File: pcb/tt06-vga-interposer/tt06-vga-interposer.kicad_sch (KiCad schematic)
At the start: 71 parts, among them CON1 Bottom pins, CON2 Bottom pins, CON3 Top socket, CON4 Top socket, J1 Conn_02x09_Odd_Even, J2 DE15_Receptacle_HighDensity_M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, J3 Conn_01x04_Pin, J4 Conn_01x04_Pin, U1 OPA3355EA, U2 SN74ALVC245DWR

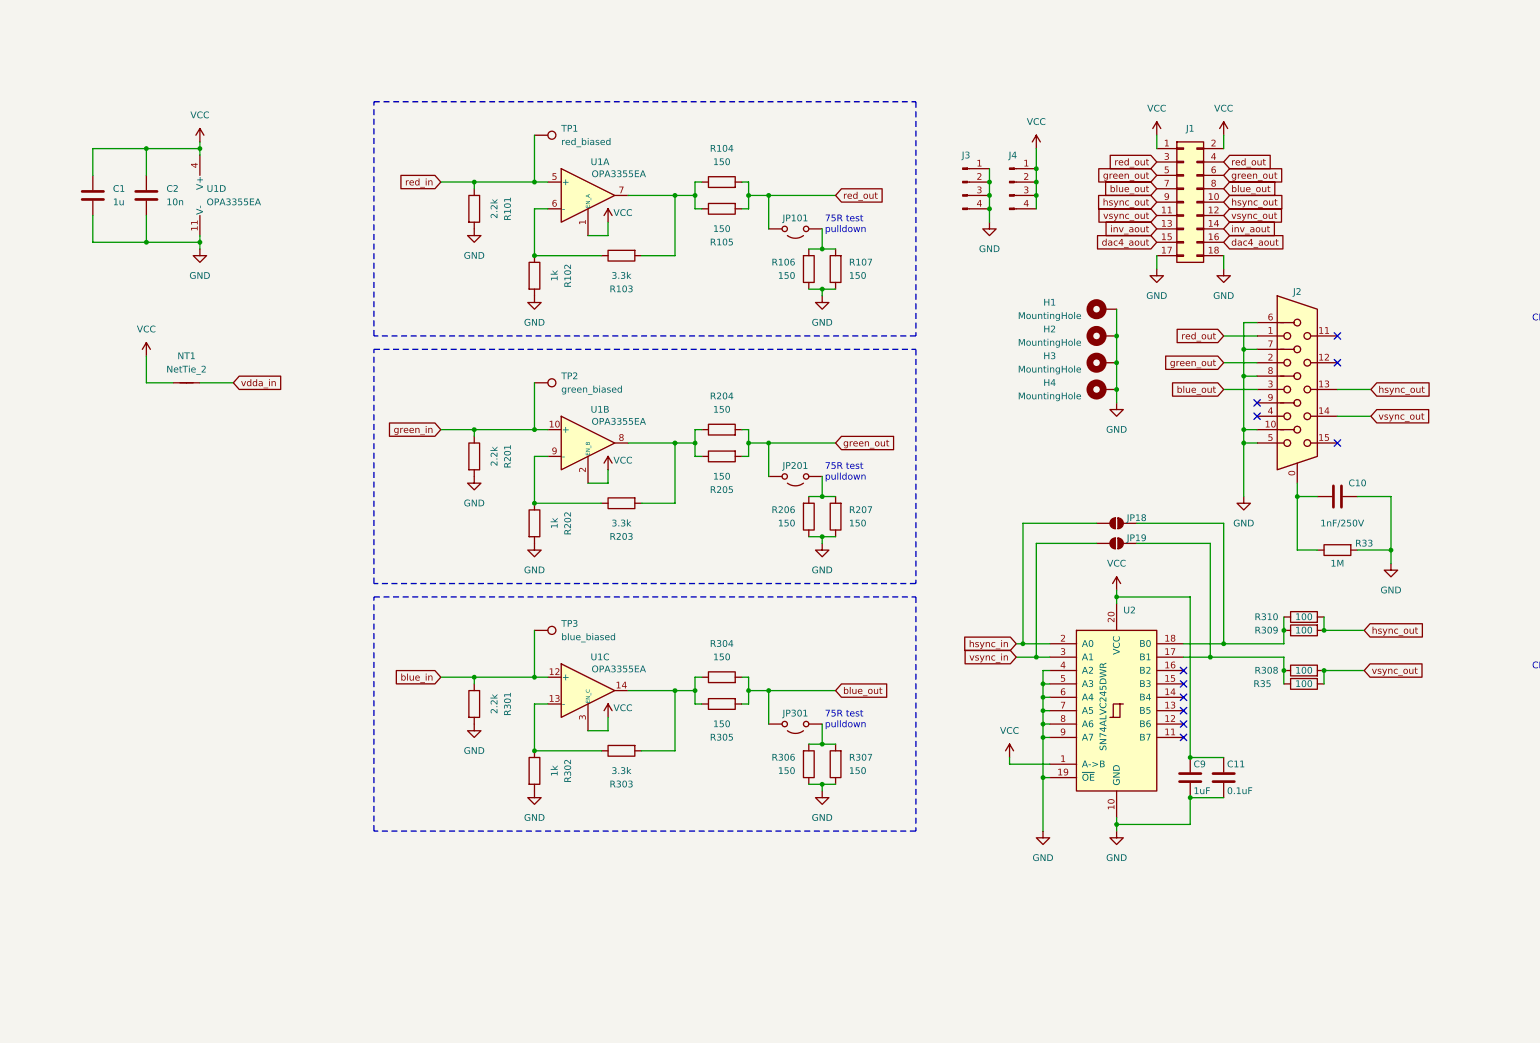
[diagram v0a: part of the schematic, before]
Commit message: Partial layout of interposer PCB
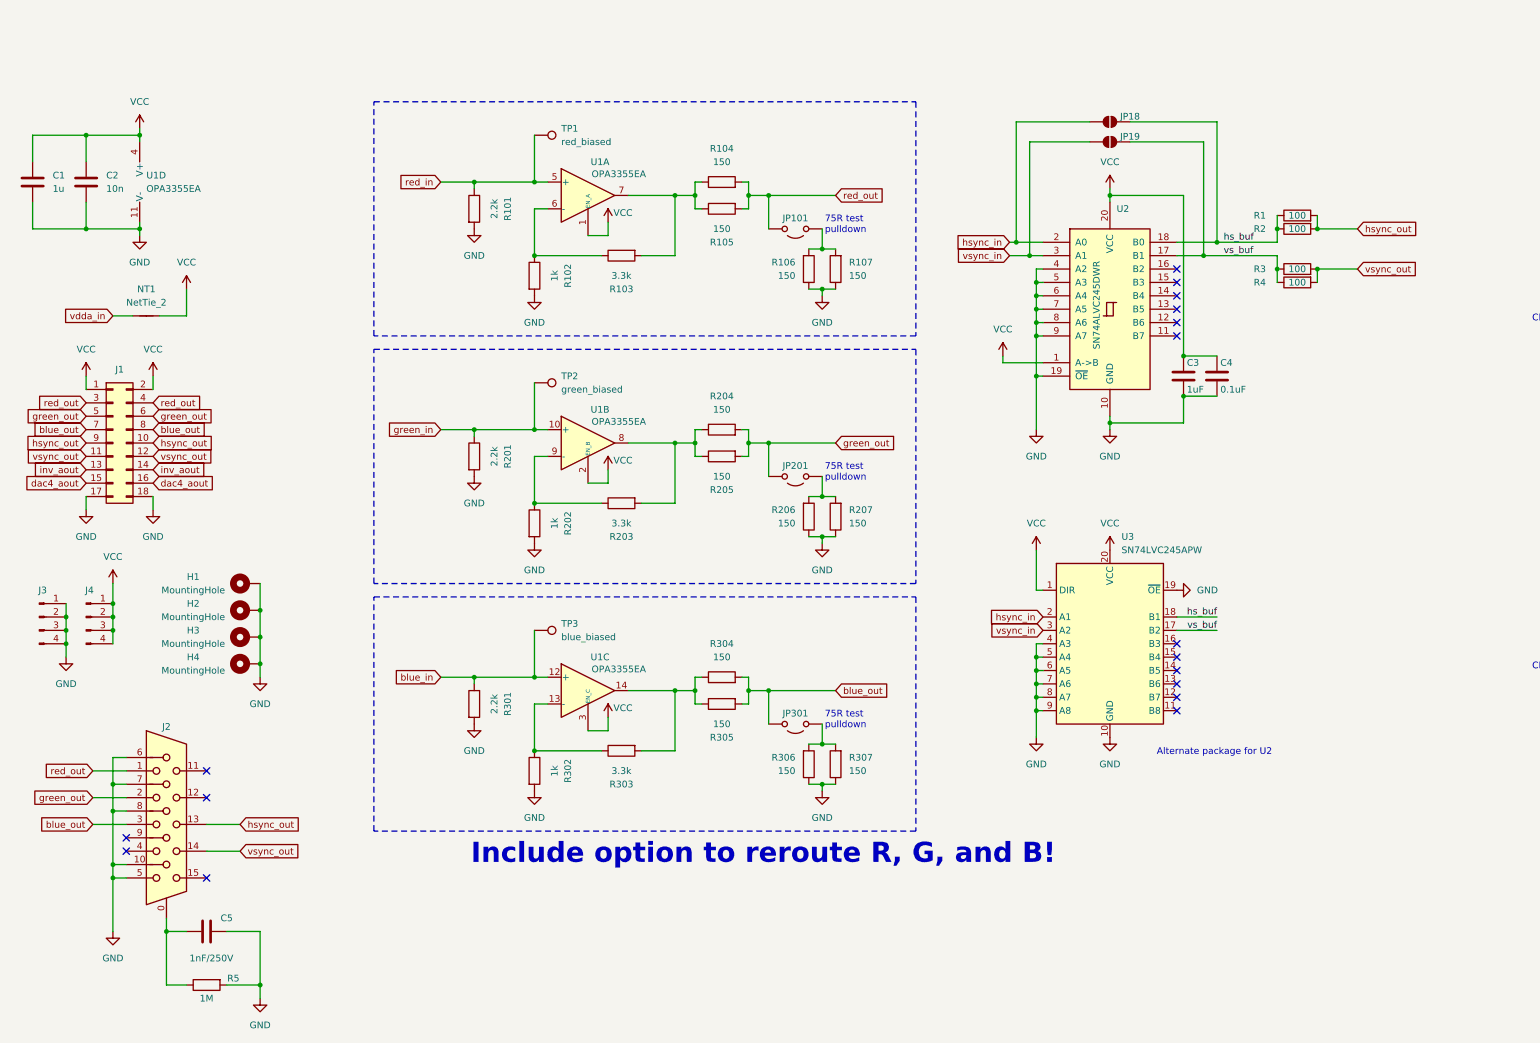
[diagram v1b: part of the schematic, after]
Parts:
- added U3: SN74LVC245APW, Anton Kicad Footprints Lib:TSSOP-20_4.4x6.5mm_P0.65mm_HandSolder, symbol Logic_LevelTranslator:SN74LVC245APW
- J1: footprint (none) -> Connector_PinHeader_2.54mm:PinHeader_2x09_P2.54mm_Horizontal
- renumbered C9 to C3, C11 to C4, C10 to C5, R310 to R1, R309 to R2, R308 to R3, R35 to R4, R33 to R5
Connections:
- net GND: now also U3.10 (GND), U3.19 (~{OE}), U3.4 (A3), U3.5 (A4), U3.6 (A5), U3.7 (A6), U3.8 (A7), U3.9 (A8)
- net VCC: now also U3.1 (DIR), U3.20 (VCC)
- net hsync_in: now also U3.2 (A1)
- net vsync_in: now also U3.3 (A2)
- net vs_buf: now reaches JP19.2 (B), R3.1, R4.1, U2.17 (B1)
- net vs_buf: now also U3.17 (B2)
- net hs_buf: now reaches JP18.2 (B), R1.1, R2.1, U2.18 (B0)
- net hs_buf: now also U3.18 (B1)
- no-connect marks 11 -> 17
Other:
- note added: "Alternate package for U2"
- note added: "Include option to reroute R, G, and B!"
- moved on the sheet: C1, C2, C3, C4, C5, H1, H2, H3, H4, J1, J2, J3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

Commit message: Nearly finished 1st draft of interposer PCB
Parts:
- removed JP13, JP14: SolderJumper_2_Open, Anton Kicad Footprints Lib:SolderJumper-2_tiny_nomask, symbol Jumper:SolderJumper_2_Open
- removed U2: SN74ALVC245DWR, Package_SO:SOIC-20W_7.5x12.8mm_P1.27mm, symbol Anton Kicad Symbols Lib:SN74ALVC245DWR
- added J5: Conn_02x07_Odd_Even, Connector_PinHeader_2.54mm:PinHeader_2x07_P2.54mm_Horizontal, symbol Connector_Generic:Conn_02x07_Odd_Even
- added JP16: SolderJumper_2_Open, Anton Kicad Footprints Lib:SolderJumper-2_tiny_nomask, symbol Jumper:SolderJumper_2_Open
- added NT2, NT3: NetTie_2, NetTie:NetTie-2_SMD_Pad0.5mm, symbol Device:NetTie_2
- JP101, JP201, JP301, R106, R107, R206, R207, R306, R307, TP1, TP2, TP3: now not fitted
- renumbered JP16 to JP13, JP17 to JP14, JP18 to JP17, JP19 to JP18, U3 to U2
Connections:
- net GND: now also J1.1 (Pin_1), J1.2 (Pin_2); no longer J1.17 (Pin_17), J1.18 (Pin_18)
- net VCC: now also J1.17 (Pin_17), J1.18 (Pin_18); no longer J1.1 (Pin_1), J1.2 (Pin_2)
- net blue_in: now also J5.11 (Pin_11); no longer JP15.2 (B)
- net blue_out: now also J1.11 (Pin_11), J1.12 (Pin_12); no longer J1.7 (Pin_7), J1.8 (Pin_8)
- net chip_an0: now also J5.12 (Pin_12), J5.4 (Pin_4), J5.8 (Pin_8)
- net chip_an4: now also J5.13 (Pin_13), J5.5 (Pin_5); no longer JP15.1 (A)
- net chip_an5: now also J5.1 (Pin_1), J5.9 (Pin_9)
- net dac4_aout: now also J1.5 (Pin_5), J1.6 (Pin_6); no longer J1.15 (Pin_15), J1.16 (Pin_16)
- net green_in: now also J5.7 (Pin_7)
- net green_out: now also J1.13 (Pin_13), J1.14 (Pin_14); no longer J1.5 (Pin_5), J1.6 (Pin_6)
- net hsync_in: now also JP15.2 (B), NT2.2; no longer JP17.1 (A), U2.2 (A1)
- net hsync_out: now also J1.7 (Pin_7), J1.8 (Pin_8); no longer J1.10 (Pin_10), J1.9 (Pin_9)
- net inv_aout: now also J1.3 (Pin_3), J1.4 (Pin_4); no longer J1.13 (Pin_13), J1.14 (Pin_14)
- net red_in: now also J5.3 (Pin_3)
- net red_out: now also J1.15 (Pin_15), J1.16 (Pin_16); no longer J1.3 (Pin_3), J1.4 (Pin_4)
- net uout3: now also NT3.1
- net uout7: now also NT2.1
- net vsync_in: now also JP16.2 (B), NT3.2; no longer JP18.1 (A), U2.3 (A2)
- net vsync_out: now also J1.10 (Pin_10), J1.9 (Pin_9); no longer J1.11 (Pin_11), J1.12 (Pin_12)
- new net: JP16.1 (A), JP18.1 (A), U2.3 (A2)
- new net: JP15.1 (A), JP17.1 (A), U2.2 (A1)
- no-connect marks 17 -> 15
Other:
- note added: "1=A->B"
- note removed: "Alternate package for U2"
- moved on the sheet: C3, C4, JP17, JP18, R1, R2, R3, R4, U2

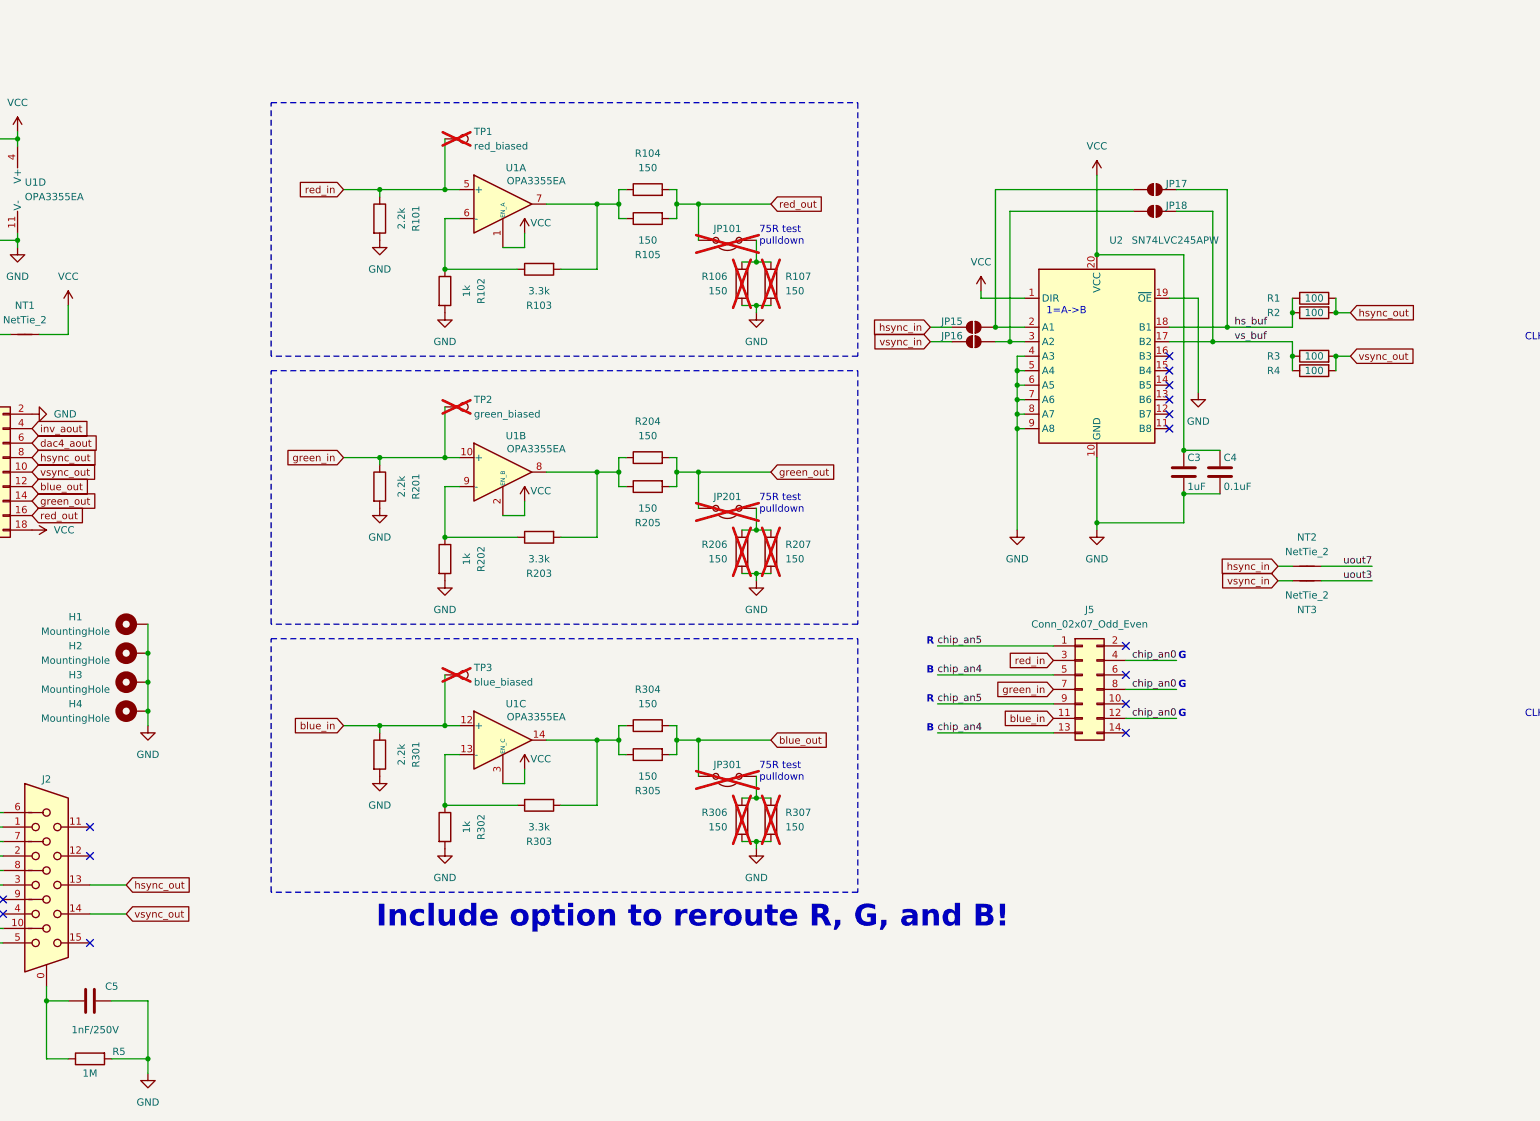
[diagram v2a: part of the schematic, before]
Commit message: Interposer PCB: First complete version
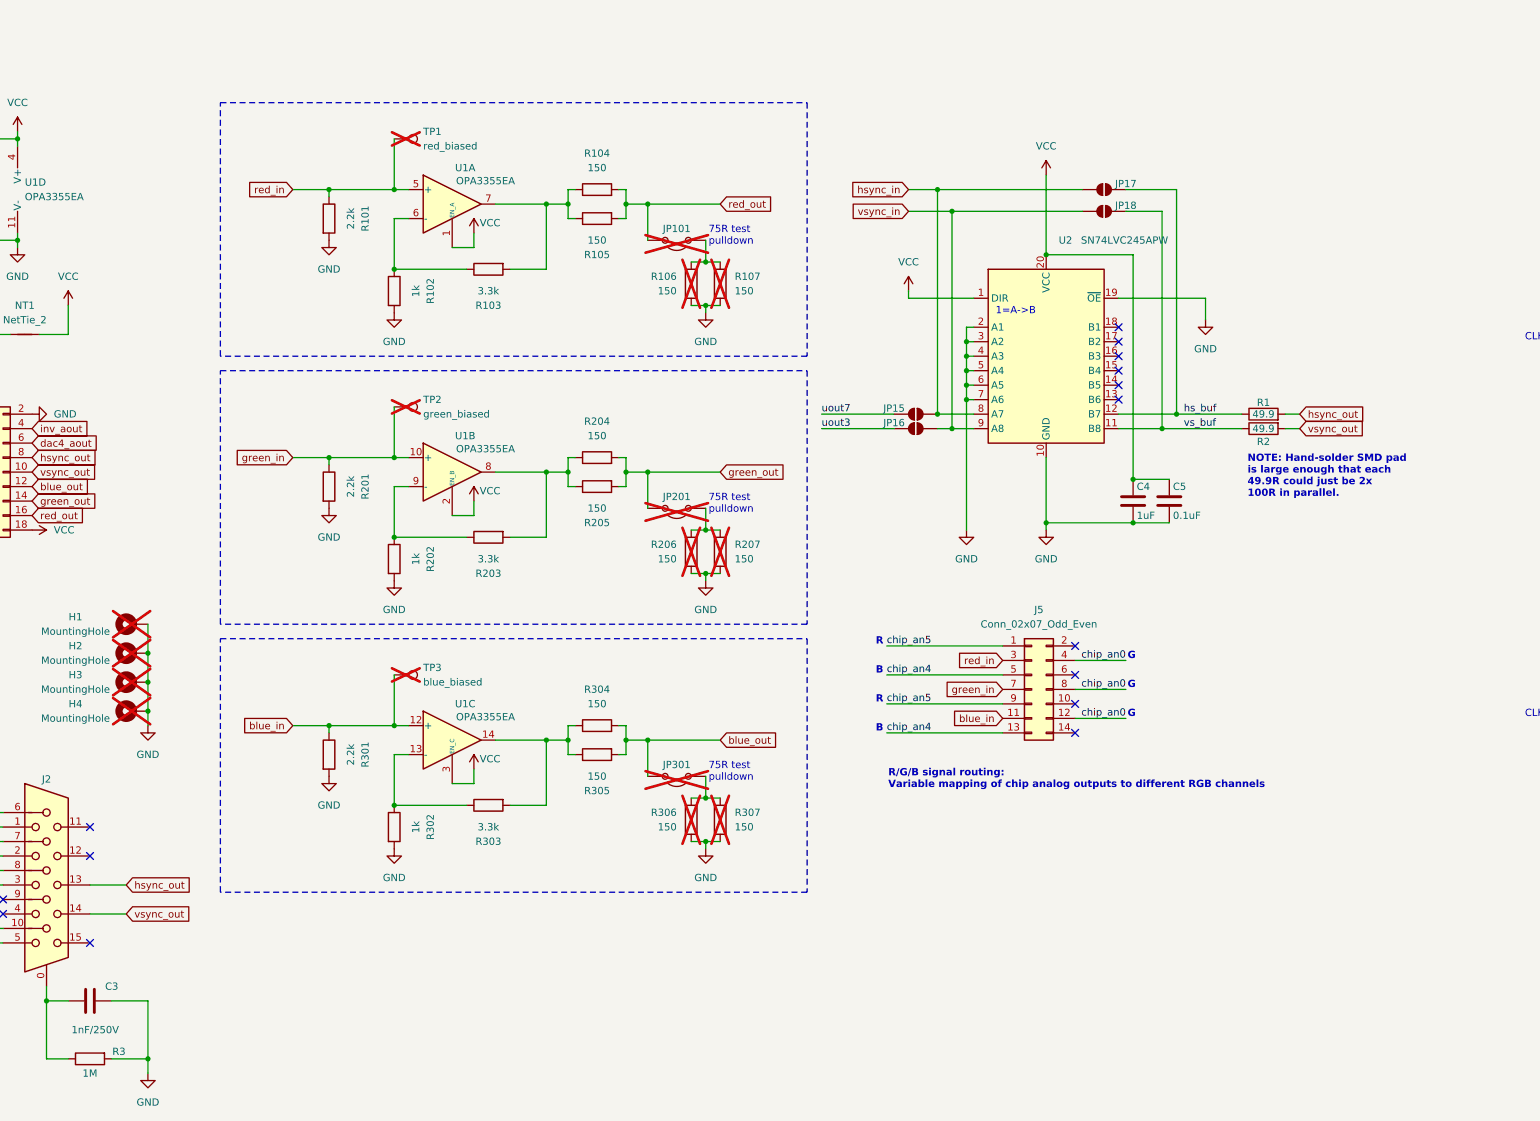
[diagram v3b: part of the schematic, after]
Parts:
- removed NT2, NT3: NetTie_2, NetTie:NetTie-2_SMD_Pad0.5mm, symbol Device:NetTie_2
- removed R3, R4: 100, Anton Kicad Footprints Lib:SMD_Passive_HandSolder_0603_to_1210, symbol Device:R
- H1, H2, H3, H4: now not fitted
- J1: footprint Connector_PinHeader_2.54mm:PinHeader_2x09_P2.54mm_Horizontal -> Connector_PinHeader_2.54mm:PinHeader_2x09_P2.54mm_Vertical
- R1, R2: value 100 -> 49.9
- renumbered C5 to C3, C3 to C4, C4 to C5, R5 to R3
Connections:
- net GND: now also U2.2 (A1), U2.3 (A2); no longer U2.8 (A7), U2.9 (A8)
- net hs_buf: now also U2.12 (B7); no longer R2.1, U2.18 (B1)
- net hsync_in: now also JP15.1 (A), JP17.1 (A), U2.8 (A7); no longer JP15.2 (B)
- net hsync_out: no longer R2.2
- net uout3: now also JP16.2 (B)
- net uout7: now also JP15.2 (B)
- net vs_buf: now also R2.1, U2.11 (B8); no longer U2.17 (B2)
- net vsync_in: now also JP16.1 (A), JP18.1 (A), U2.9 (A8); no longer JP16.2 (B)
- net vsync_out: now also R2.2
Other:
- note added: "NOTE: Hand-solder SMD pad is large enough that each 49.9R could just be 2x 100R in parallel."
- note added: "R/G/B signal routing: Variable mapping of chip analog outputs to different RGB channels"
- note removed: "Include option to reroute R, G, and B!"
- moved on the sheet: C4, C5, J5, JP101, JP15, JP16, JP17, JP18, JP201, JP301, R1, R101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

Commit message: Tidy up interposer schematic a little
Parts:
- removed H1, H2, H3, H4: MountingHole, MountingHole:MountingHole_4.3mm_M4_DIN965_Pad, symbol Mechanical:MountingHole_Pad
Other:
- note added: "NOTE: R1/R2 hand-solder SMD pad is large enough that each 49.9R could just be 2x 100R in parallel."
- note removed: "NOTE: Hand-solder SMD pad is large enough that each 49.9R could just be 2x 100R in parallel."
- moved on the sheet: C1, C2, C3, C4, C5, CON1, CON2, CON3, CON4, J1, J2, J3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
